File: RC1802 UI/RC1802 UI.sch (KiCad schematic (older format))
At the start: 65 parts, among them J1 CONN_01X39, J2 BARREL_JACK, J3 Mount, J4 Mount, J5 Mount, J6 Mount, SW1 CLEAR, SW10 IN5, SW11 IN6, SW12 IN7, SW2 IN, SW3 MP, SW4 WAIT, SW5 IN0, SW6 IN1, SW7 IN2, SW8 IN3, SW9 IN4, U1 CDP1802, U10 MC14495P1, U11 28C256, U2 74LS373, U3 HM62256BLP-7, U4 74LS04, U5 4050, U6 4013, U7 74LS10, U8 MC14495P1, U9 74LS245, X1 CXO_DIP14

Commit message: Completed front panel with exports.
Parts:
- removed C10, C11, C8, C9: 100nF, Capacitors_THT:C_Disc_D4.7mm_W2.5mm_P5.00mm, symbol C_Small
- removed J2: BARREL_JACK, Connectors:BARREL_JACK, symbol BARREL_JACK
- removed JP1: U12 WE, Pin_Headers:Pin_Header_Straight_1x03_Pitch2.54mm, symbol Jumper_NC_Dual
- removed JP2: Enable, Pin_Headers:Pin_Header_Straight_1x02_Pitch2.54mm, symbol Jumper_NC_Small
- removed JP3: HI, Pin_Headers:Pin_Header_Straight_1x03_Pitch2.54mm, symbol Jumper_NC_Dual
- removed JP4: LO, Pin_Headers:Pin_Header_Straight_1x03_Pitch2.54mm, symbol Jumper_NC_Dual
- removed R1, R2, R3, R4, R5, R6, R7: 47k, Resistors_THT:R_Axial_DIN0207_L6.3mm_D2.5mm_P10.16mm_Horizontal, symbol R
- removed U1: CDP1802, Housings_DIP:DIP-40_W15.24mm_Socket, symbol CDP1802
- removed U11: 28C256, Housings_DIP:DIP-32_W15.24mm_Socket, symbol 28C256
- removed U2: 74LS373, Housings_DIP:DIP-20_W7.62mm_Socket, symbol 74LS373
- removed U3: HM62256BLP-7, Housings_DIP:DIP-32_W15.24mm_Socket, symbol HM62256BLP-7
- removed unit 6 of U4
- removed X1: CXO_DIP14, Oscillators:Oscillator_DIP-14, symbol CXO_DIP14
- added J6: CONN_02X20, Connectors:IDC_Header_Straight_40pins, symbol CONN_02X20
- renumbered J3 to J1, J4 to J2, J5 to J3, J6 to J4, J1 to J5, R10 to R1, R8 to R2, R9 to R3, U4 to U1, U5 to U2, U6 to U3, U7 to U4, U8 to U5, U9 to U6, U10 to U7
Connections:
- net LOAD is gone; now on net ~CLEAR: J5.19 (P19)
- net WAIT is gone; now on net ~WAIT: D3.2 (A), U1.11, U1.6
- net ~WE is gone; now on net MP: SW3.2 (B)
- net BUS0: now also J6.19 (P19)
- net BUS1: now also J6.17 (P17)
- net BUS2: now also J6.15 (P15)
- net BUS3: now also J6.13 (P13)
- net BUS4: now also J6.11 (P11)
- net BUS5: now also J6.9 (P9)
- net BUS6: now also J6.7 (P7)
- net BUS7: now also J6.5 (P5)
- net DMA_IN: now also J6.33 (P33)
- net EF4: now also J6.27 (P27)
- net GND: now also J6.10 (P10), J6.12 (P12), J6.14 (P14), J6.16 (P16), J6.18 (P18), J6.20 (P20), J6.22 (P22), J6.24 (P24), J6.26 (P26), J6.28 (P28), J6.30 (P30), J6.32 (P32), J6.34 (P34), J6.36 (P36), J6.38 (P38), J6.4 (P4), J6.40 (P40), J6.6 (P6), J6.8 (P8)
- net MRD: now also J6.37 (P37)
- net MWR: now also J6.39 (P39)
- net N2: now also J6.35 (P35)
- net Q: now also J6.25 (P25)
- net SC1: now also J6.29 (P29)
- net TPB: now also J6.31 (P31)
- net VCC: now also J6.2 (P2)
- net MP: now reaches J5.26 (P26)
- net MP: now also J6.3 (P3)
- net CLEAR renamed ~CLEAR
- net ~CLEAR: now also J6.21 (P21)
- net CLOCK: no longer names the net of J5.21 (P21)
- net DMA_OUT: no longer names the net of J5.35 (P35)
- net EF1: no longer names the net of J5.1 (P1)
- net EF2: no longer names the net of J5.2 (P2)
- net EF3: no longer names the net of J5.3 (P3)
- net INTERRUPT: no longer names the net of J5.22 (P22)
- net MA0: no longer names the net of J5.16 (P16)
- net MA1: no longer names the net of J5.15 (P15)
- net MA2: no longer names the net of J5.14 (P14)
- net MA3: no longer names the net of J5.13 (P13)
- net MA4: no longer names the net of J5.12 (P12)
- net MA5: no longer names the net of J5.11 (P11)
- net MA6: no longer names the net of J5.10 (P10)
- net MA7: no longer names the net of J5.9 (P9)
- net N0: no longer names the net of J5.39 (P39)
- net N1: no longer names the net of J5.38 (P38)
- net RUN renamed ~WAIT
- net ~WAIT: now also J6.23 (P23)
- net SC0: no longer names the net of J5.6 (P6)
- net TPA: no longer names the net of J5.8 (P8)
- no-connect marks 15 -> 31
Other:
- moved on the sheet: AFF1, AFF2, U5, U7

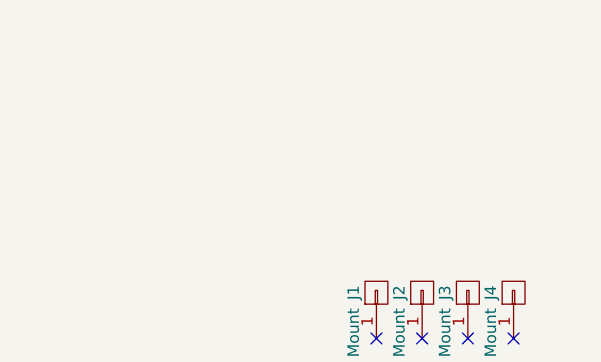
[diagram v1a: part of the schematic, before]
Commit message: Connected VSS and GND
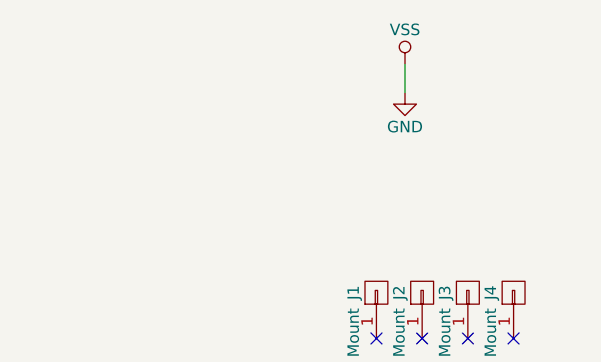
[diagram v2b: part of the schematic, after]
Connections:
- net VSS is gone; now on net GND: U2.8 (VSS), U2.8 (VSS)
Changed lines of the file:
@@
 	13875 6425 13950 6425
 Connection ~ 13950 6425
+$Comp
+L GND #PWR?
+U 1 1 5B8B4060
+P 15275 850
+F 0 "#PWR?" H 15275 600 50  0001 C CNN
+F 1 "GND" H 15275 700 50  0000 C CNN
+F 2 "" H 15275 850 50  0001 C CNN
+F 3 "" H 15275 850 50  0001 C CNN
+	1    15275 850
+	1    0    0    -1
+$EndComp
+$Comp
+L VSS #PWR?
+U 1 1 5B8B40DC
+P 15275 725
+F 0 "#PWR?" H 15275 575 50  0001 C CNN
+F 1 "VSS" H 15275 875 50  0000 C CNN
+F 2 "" H 15275 725 50  0001 C CNN
+F 3 "" H 15275 725 50  0001 C CNN
+	1    15275 725
+	1    0    0    -1
+$EndComp
+Wire Wire Line
+	15275 850  15275 725
 $EndSCHEMATC

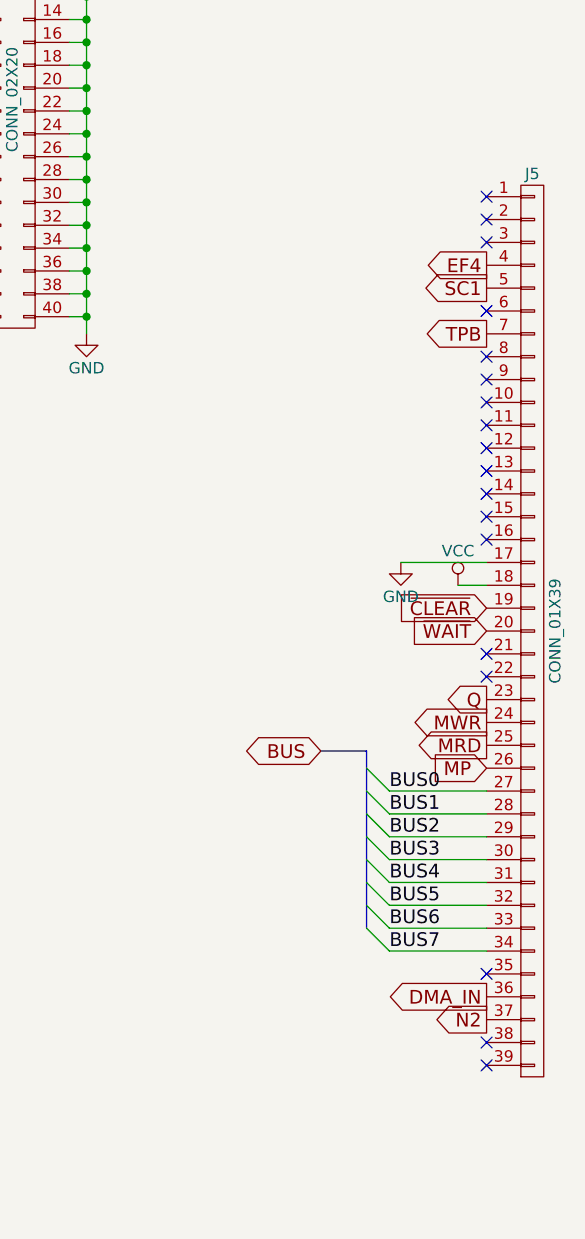
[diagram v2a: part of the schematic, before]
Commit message: Removed backplane connector and cleanup
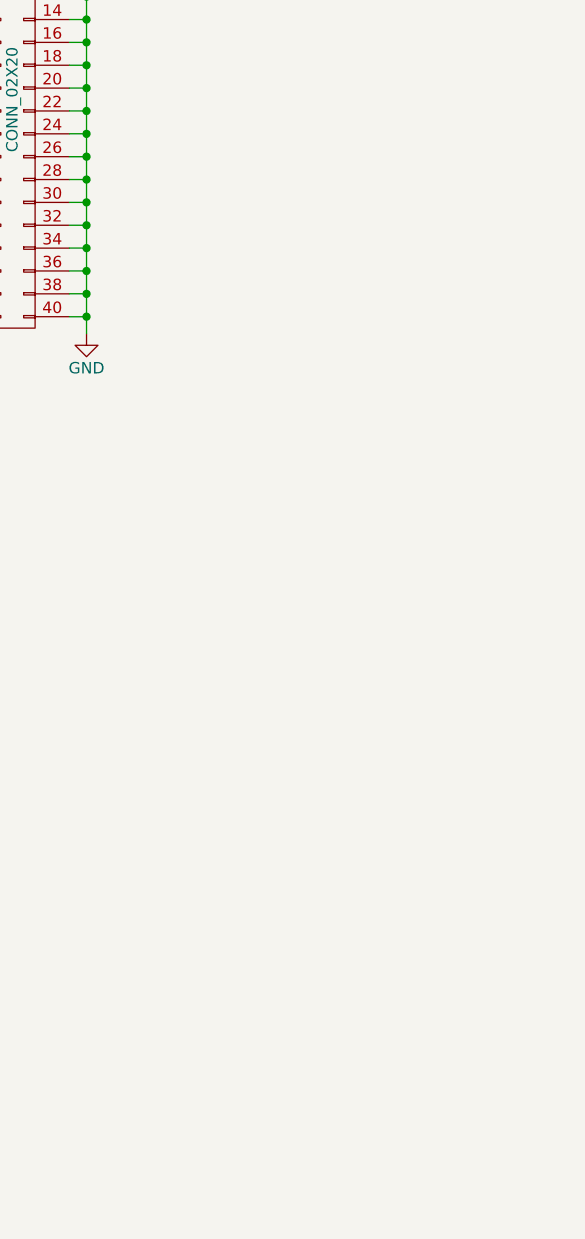
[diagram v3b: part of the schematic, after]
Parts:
- removed J5: CONN_01X39, Pin_Headers:Pin_Header_Angled_1x39_Pitch2.54mm, symbol CONN_01X39
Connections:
- no-connect marks 31 -> 13
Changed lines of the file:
@@
 $EndDescr
-$Comp
-L CONN_01X39 J5
-U 1 1 5945F778
-P 15900 7800
-F 0 "J5" H 15900 9800 50  0000 C CNN
-F 1 "CONN_01X39" V 16000 7800 50  0000 C CNN
-F 2 "Pin_Headers:Pin_Header_Angled_1x39_Pitch2.54mm" H 15900 7800 50  0001 C CNN
-F 3 "" H 15900 7800 50  0001 C CNN
-	1    15900 7800
-	1    0    0    -1
-$EndComp
-Entry Wire Line
-	15175 8600 15275 8700
-Entry Wire Line
-	15175 8500 15275 8600
-Entry Wire Line
-	15175 8400 15275 8500
-Entry Wire Line
-	15175 8700 15275 8800
-Entry Wire Line
-	15175 8800 15275 8900
-Entry Wire Line
-	15175 8900 15275 9000
-Entry Wire Line
-	15175 9000 15275 9100
-Entry Wire Line
-	15175 9100 15275 9200
-Text Label 15275 8500 0    60   ~ 0
-BUS0
-Text Label 15275 8600 0    60   ~ 0
-BUS1
-Text Label 15275 8700 0    60   ~ 0
-BUS2
-Text Label 15275 8800 0    60   ~ 0
-BUS3
-Text Label 15275 8900 0    60   ~ 0
-BUS4
-Text Label 15275 9000 0    60   ~ 0
-BUS5
-Text Label 15275 9100 0    60   ~ 0
-BUS6
-Text Label 15275 9200 0    60   ~ 0
-BUS7
-$Comp
-L VCC #PWR01
-U 1 1 5946201E
-P 15575 7600
-F 0 "#PWR01" H 15575 7450 50  0001 C CNN
-F 1 "VCC" H 15575 7750 50  0000 C CNN
-F 2 "" H 15575 7600 50  0001 C CNN
-F 3 "" H 15575 7600 50  0001 C CNN
-	1    15575 7600
-	1    0    0    -1
-$EndComp
-$Comp
-L GND #PWR02
-U 1 1 5946208C
-P 15325 7500
-F 0 "#PWR02" H 15325 7250 50  0001 C CNN
-F 1 "GND" H 15325 7350 50  0000 C CNN
-F 2 "" H 15325 7500 50  0001 C CNN
-F 3 "" H 15325 7500 50  0001 C CNN
-	1    15325 7500
-	1    0    0    -1
-$EndComp
-Text GLabel 14975 8325 0    60   BiDi ~ 0
-BUS
-Text GLabel 15700 6200 0    60   Output ~ 0
-EF4
-Text GLabel 15700 8100 0    60   Output ~ 0
-Q
-Text GLabel 15700 6300 0    60   Output ~ 0
-SC1
-Text GLabel 15700 7700 0    60   Input ~ 0
-~CLEAR
-Text GLabel 15700 7800 0    60   Input ~ 0
-~WAIT
-Text GLabel 15700 9500 0    60   Output ~ 0
-N2
-Text GLabel 15700 8300 0    60   Output ~ 0
-MRD
-Text GLabel 15700 8200 0    60   Output ~ 0
-MWR
-Text GLabel 15700 6500 0    60   Output ~ 0
-TPB
-Text GLabel 15700 9400 0    60   Output ~ 0
-DMA_IN
 $Comp
 L 4050 U2
@@
 NoConn ~ -625 2850
 Wire Wire Line
-	15700 8500 15275 8500
-Wire Wire Line
-	15275 8600 15700 8600
-Wire Wire Line
-	15275 8700 15700 8700
-Wire Wire Line
-	15275 8800 15700 8800
-Wire Wire Line
-	15275 8900 15700 8900
-Wire Wire Line
-	15275 9000 15700 9000
-Wire Wire Line
-	15275 9100 15700 9100
-Wire Wire Line
-	15275 9200 15700 9200
-Wire Bus Line
-	15175 8325 15175 9100
-Wire Wire Line
-	15575 7600 15700 7600
-Wire Wire Line
-	15325 7500 15700 7500
-Wire Wire Line
 	1175 6425 1275 6425
 Wire Wire Line
@@
 	6775 10650 6875 10650
 Connection ~ 6775 10400
-Wire Bus Line
-	15175 8325 14975 8325
 Wire Wire Line
 	5100 8925 5100 7800
@@
 	-1   0    0    1
 $EndComp
-Text GLabel 15700 8400 0    60   Input ~ 0
-MP
-NoConn ~ 15700 9600
-NoConn ~ 15700 9700
-NoConn ~ 15700 9300
-NoConn ~ 15700 8000
-NoConn ~ 15700 7900
-NoConn ~ 15700 7400
-NoConn ~ 15700 7300
-NoConn ~ 15700 7200
-NoConn ~ 15700 7100
-NoConn ~ 15700 7000
-NoConn ~ 15700 6900
-NoConn ~ 15700 6800
-NoConn ~ 15700 6700
-NoConn ~ 15700 6600
-NoConn ~ 15700 6400
-NoConn ~ 15700 6100
-NoConn ~ 15700 6000
-NoConn ~ 15700 5900
 $Comp
 L CONN_02X20 J6

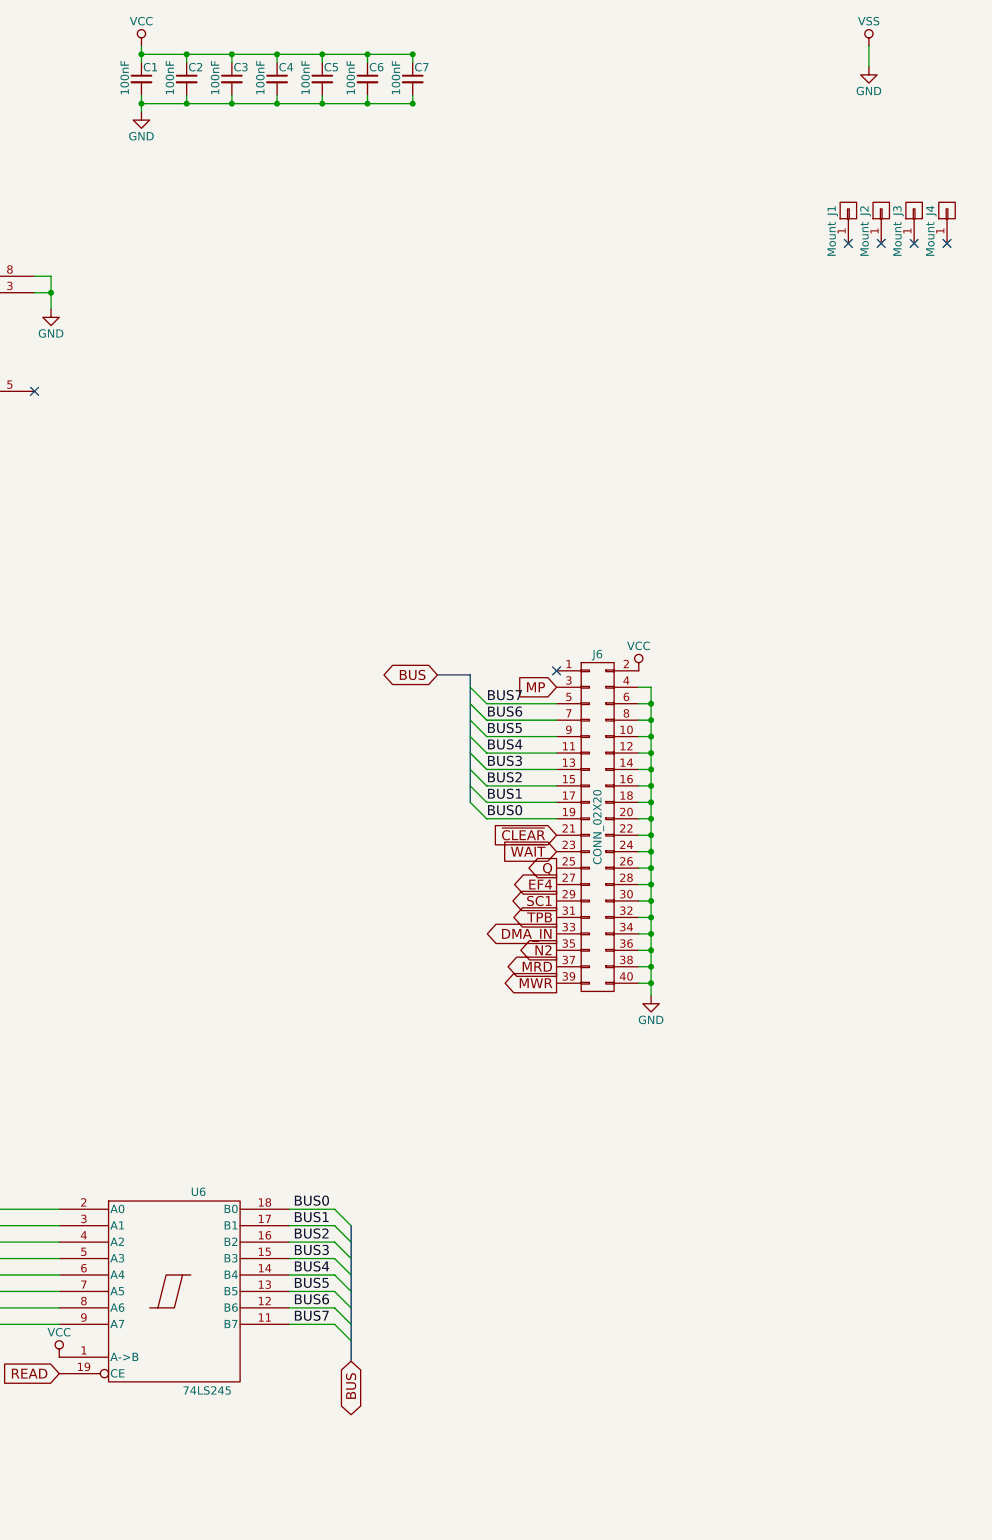
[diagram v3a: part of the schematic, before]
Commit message: Tied leftover LS04 and 4050 inputs low
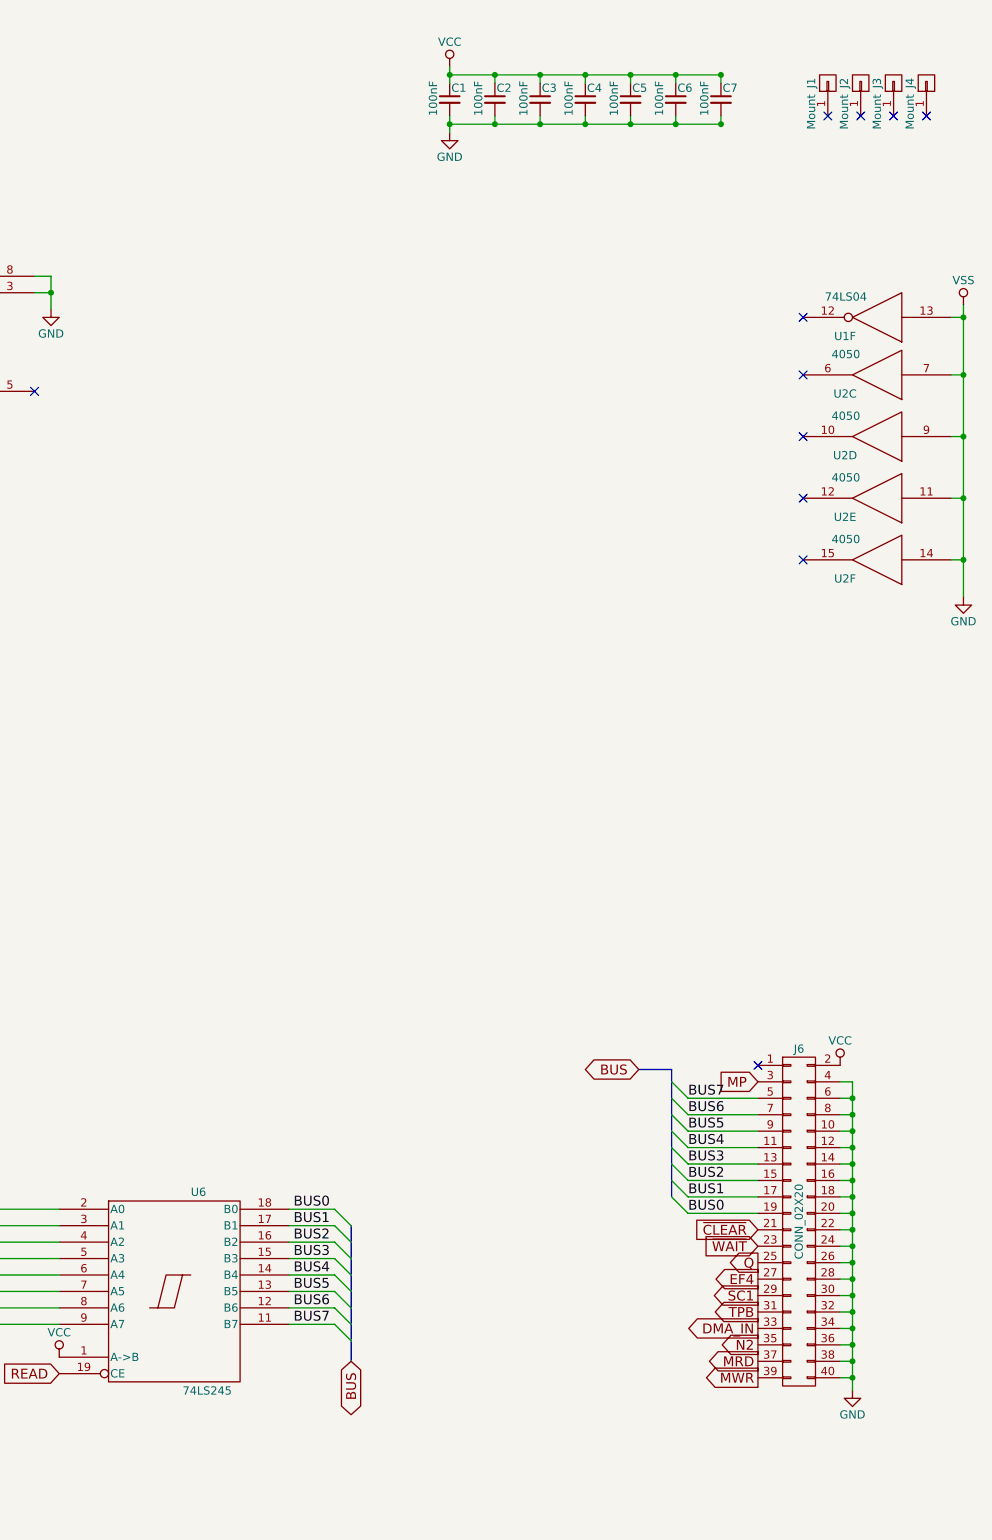
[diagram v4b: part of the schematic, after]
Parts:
- added unit 6 of U1
- added unit 4 of U2
- added unit 5 of U2
- added unit 6 of U2
- added unit 3 of U2
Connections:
- net GND: now also U1.13, U1.7 (GND), U2.11, U2.14, U2.7, U2.8 (VSS), U2.8 (VSS), U2.8 (VSS), U2.8 (VSS), U2.9
- net VCC: now also U1.14 (VCC), U2.1 (VCC), U2.1 (VCC), U2.1 (VCC), U2.1 (VCC)
- no-connect marks 13 -> 18
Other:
- moved on the sheet: C1, C2, C3, C4, C5, C6, C7, J1, J2, J3, J4, J6
